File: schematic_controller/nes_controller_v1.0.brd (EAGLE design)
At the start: 107.6 x 33 mm, 22 parts

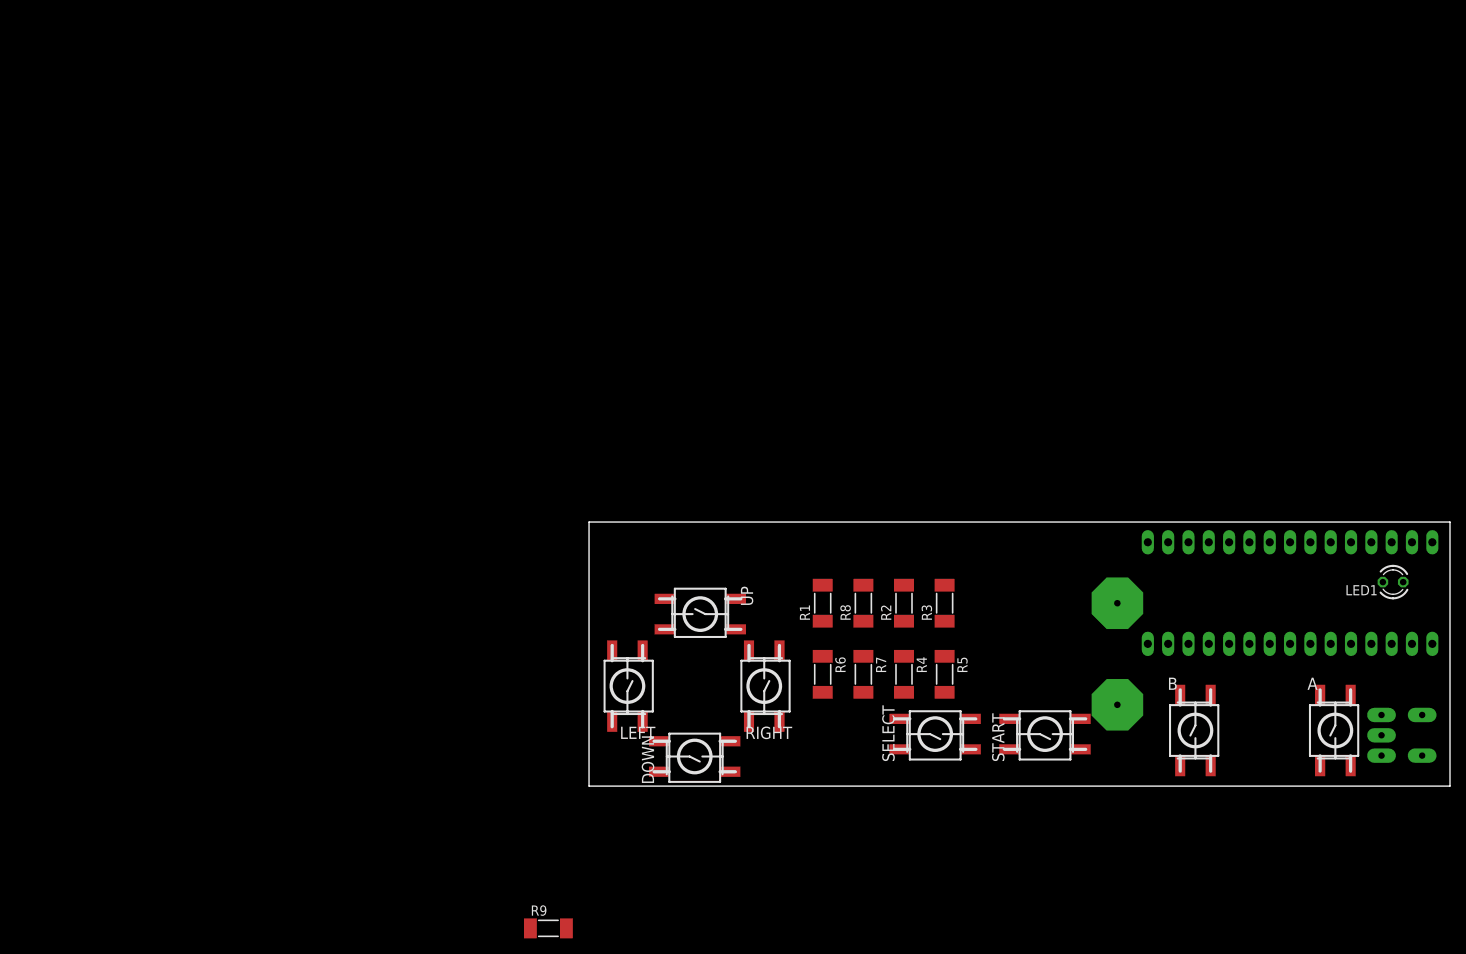
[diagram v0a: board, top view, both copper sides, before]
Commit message: updated schematic and board layout to new pin layout
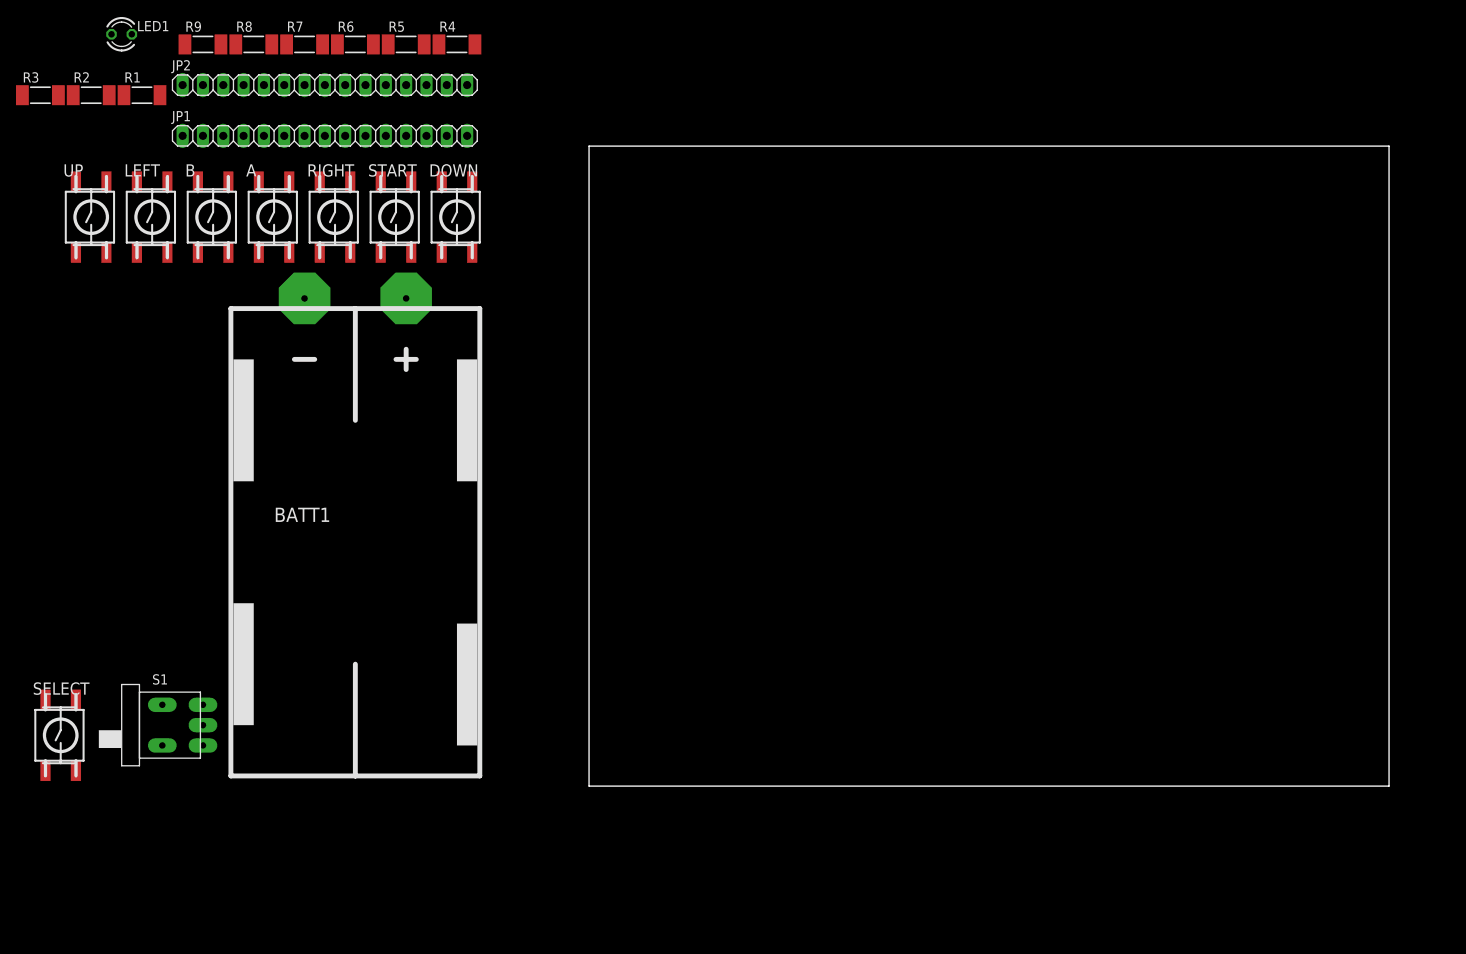
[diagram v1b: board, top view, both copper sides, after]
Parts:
- moved LED1 173.0 mm to (-58.4, 94.0), turned to 0 degrees
- moved A 147.4 mm to (-39.4, 71.1)
- moved S1 147.3 mm to (-48.3, 7.62), flipped to the top
- moved JP2 139.4 mm to (-33.0, 87.6), flipped to the top
- moved B 138.5 mm to (-47.0, 71.1)
- moved JP1 130.9 mm to (-33.0, 81.3), flipped to the top
- moved R3 129.6 mm to (-68.6, 86.4), turned to 0 degrees
- moved R2 119.8 mm to (-62.2, 86.4), turned to 0 degrees
- moved R9 118.6 mm to (-48.3, 92.7)
- moved SELECT 109.3 mm to (-66.0, 6.35), turned to 0 degrees
- moved R1 106.2 mm to (-55.9, 86.4), turned to 0 degrees
- moved R7 105.3 mm to (-35.6, 92.7), turned to 0 degrees
- moved START 103.7 mm to (-24.1, 71.1), turned to 0 degrees
- moved R5 103.6 mm to (-22.9, 92.7), turned to 0 degrees
- moved R8 103.4 mm to (-41.9, 92.7), turned to 0 degrees
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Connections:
- net A: now also JP1.5; no longer JP2.3
- net B: now also JP1.4; no longer JP2.4
- net DOWN: now also JP2.8; no longer JP2.11
- net RIGHT: now also JP2.13; no longer JP2.9
- net SELECT: now also JP2.2; no longer JP2.1
- net START: now also JP2.3; no longer JP2.2
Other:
- board size 107.6 x 33 mm -> 100 x 80 mm
